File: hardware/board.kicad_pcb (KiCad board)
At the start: 2 copper layers, 80 x 55 mm, 59 parts, among them IC1 DW01A, J1 Conn_01x04_Female, J2 Conn_01x04_Female, J3 Conn_01x04_Female, J4 Conn_01x06_Female, J5 Conn_01x14, J6 Micro_SD_Card, P1 USB_C_Plug_USB2.0, Q1 AO3401A, Q2 FS8205A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

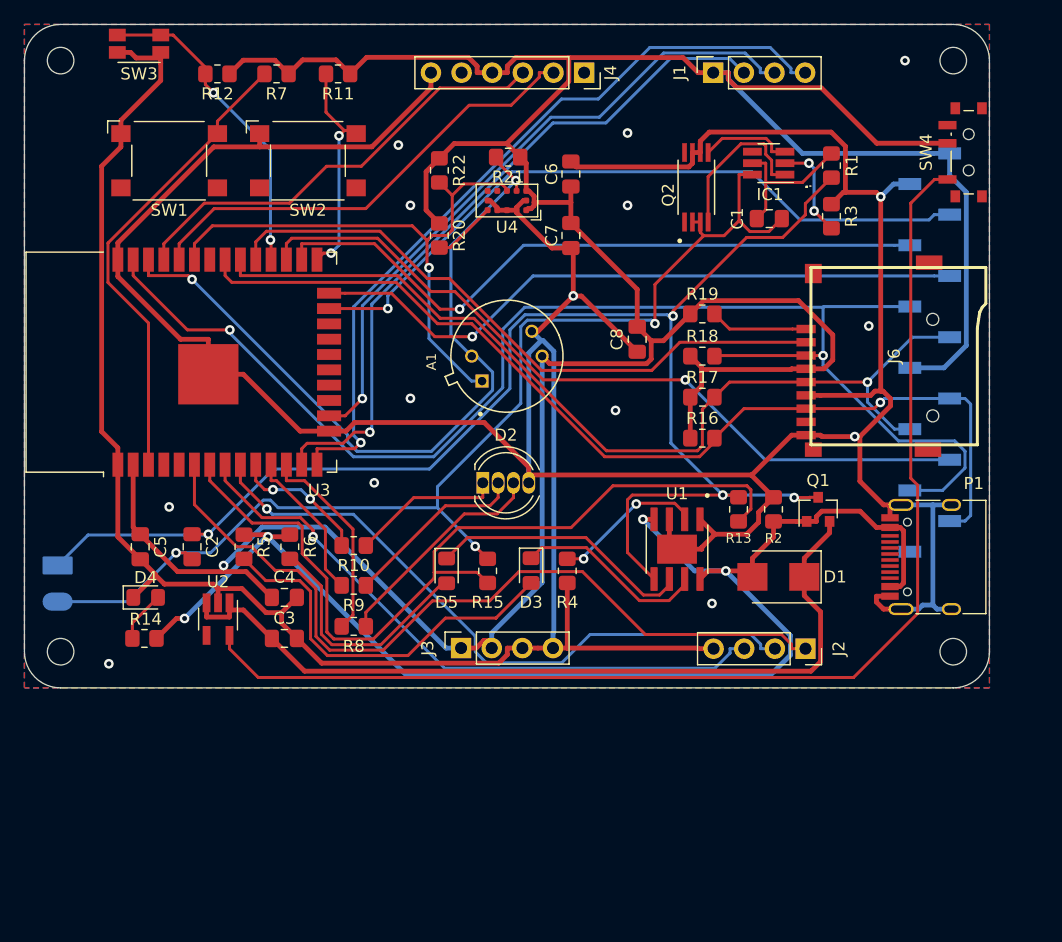
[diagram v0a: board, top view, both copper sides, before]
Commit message: Silkscreen markings added + Minor changes to tracks
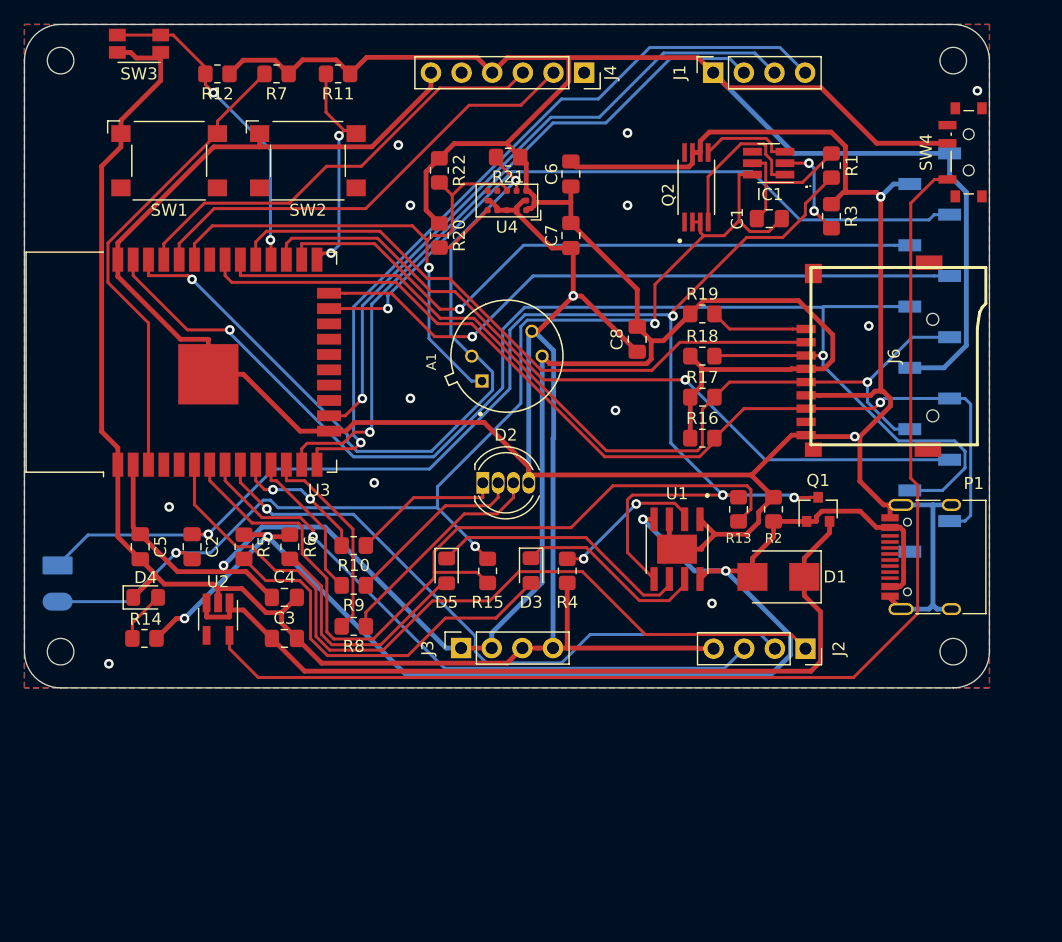
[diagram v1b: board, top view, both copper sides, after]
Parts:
- added REF**: OSHW-Logo2_7.3x6mm_SilkScreen, Symbol:OSHW-Logo2_7.3x6mm_SilkScreen, B.Cu at (111.0, 53.5)
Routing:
- net GND: track 399.5 -> 397.2 mm
- net +3V3: track 282.4 -> 281.5 mm
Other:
- board text added: "InputBlackBoxOutput"

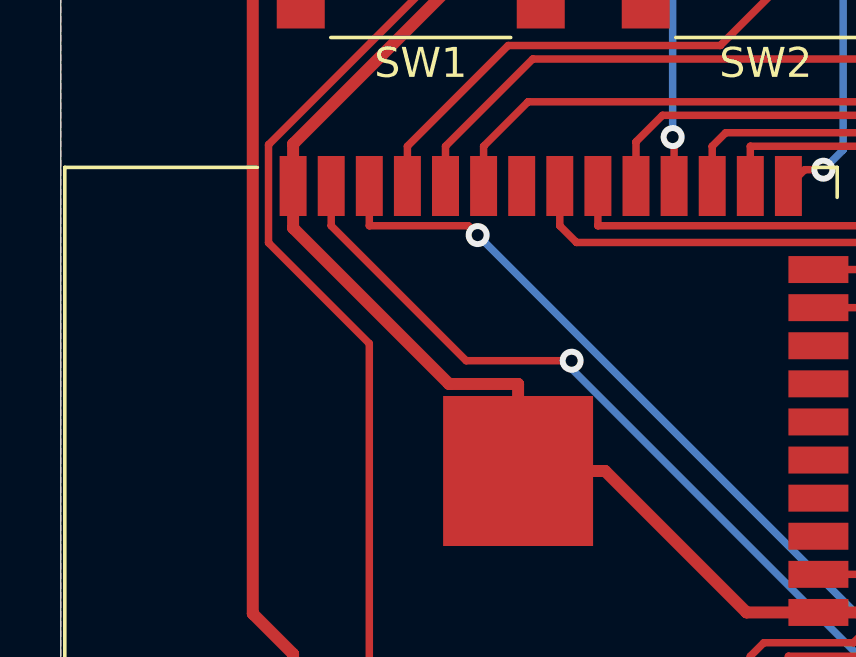
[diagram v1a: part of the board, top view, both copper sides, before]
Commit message: Minor changes to the PCB
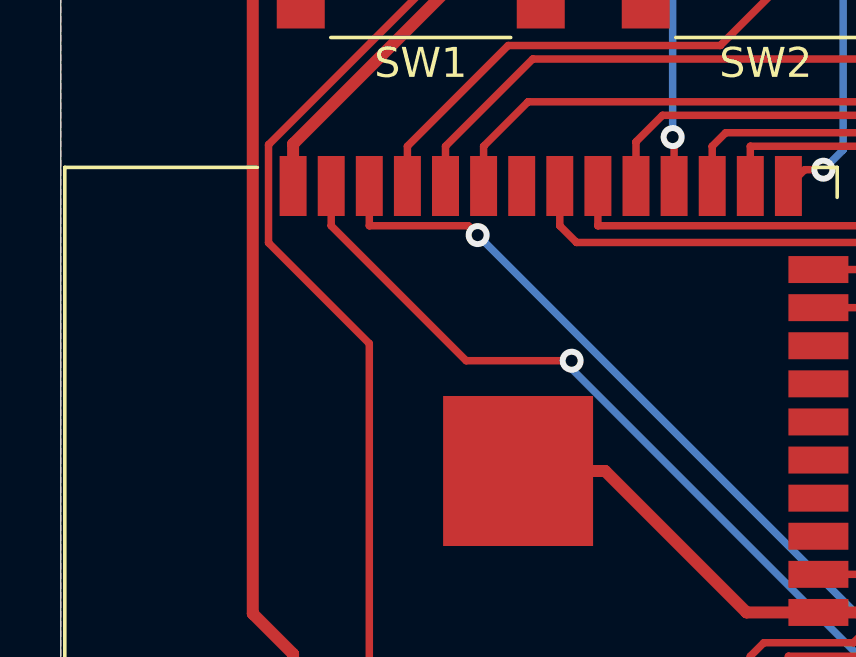
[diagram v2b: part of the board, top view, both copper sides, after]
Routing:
- net GND: track 397.2 -> 383.3 mm

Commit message: CE, FCC, WEEE and OSHW markings added to PCB
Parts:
- removed the REF** at (111.0, 53.5)
- added REF**: OSHW-Logo_5.7x6mm_SilkScreen, Symbol:OSHW-Logo_5.7x6mm_SilkScreen, B.Cu at (162.5, 64.0)
- added REF**: WEEE-Logo_4.2x6mm_SilkScreen, Symbol:WEEE-Logo_4.2x6mm_SilkScreen, B.Cu at (162.5, 70.0)
- added REF**: FCC-Logo_7.3x6mm_SilkScreen, Symbol:FCC-Logo_7.3x6mm_SilkScreen, B.Cu at (162.5, 77.0)
- added REF**: CE-Logo_8.5x6mm_SilkScreen, Symbol:CE-Logo_8.5x6mm_SilkScreen, B.Cu at (162.5, 88.0)
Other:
- board text added: "© Copyright InputBlackBoxOutput"
- board text removed: "InputBlackBoxOutput"

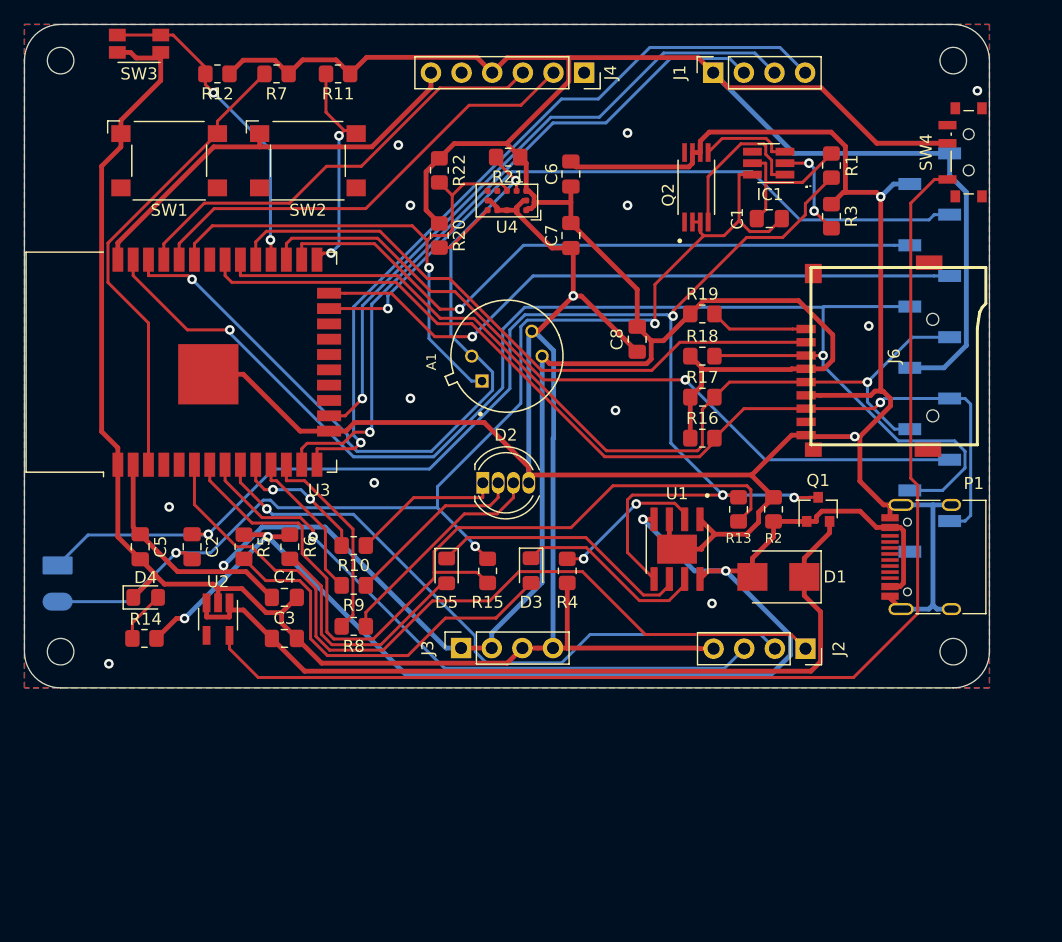
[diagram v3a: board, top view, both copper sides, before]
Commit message: Folder reorganized: hardware
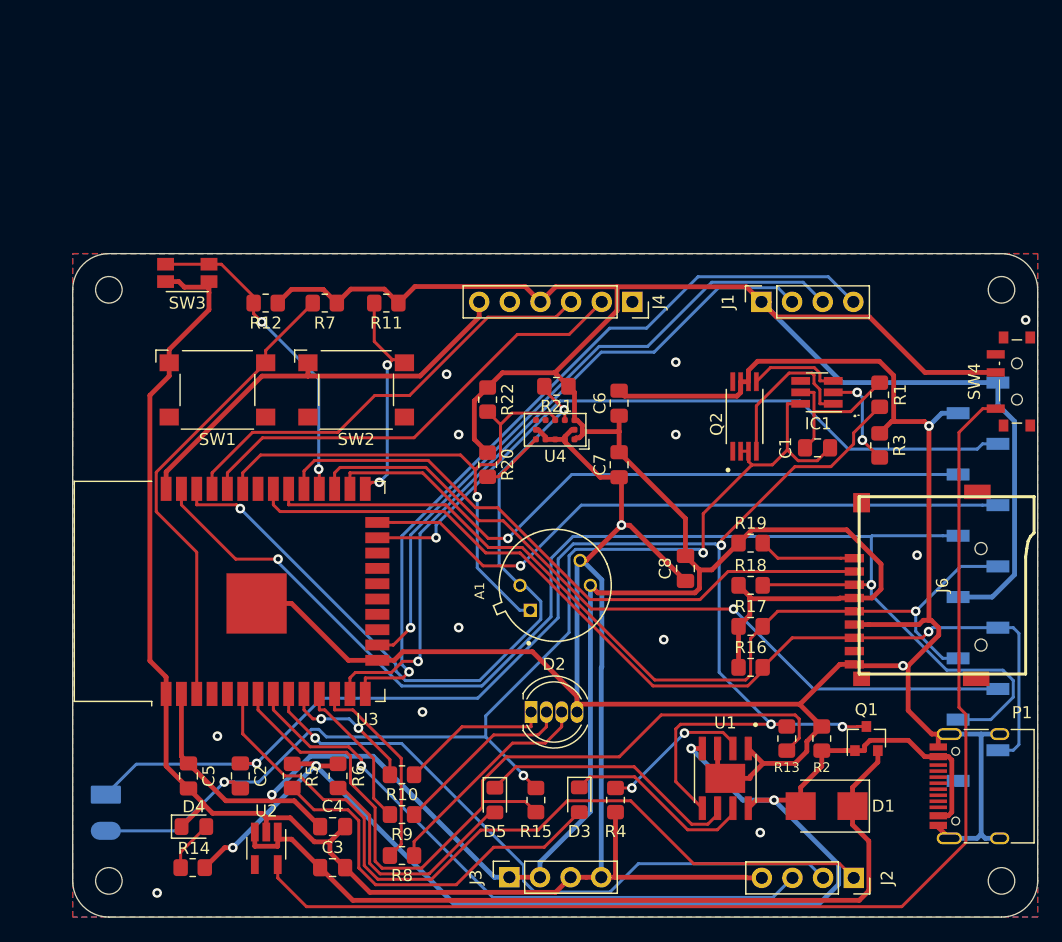
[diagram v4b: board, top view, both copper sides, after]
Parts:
- moved C6 19.4 mm to (150.3, 80.4)
- moved A1 19.4 mm to (145.0, 95.5)
- moved BT1 19.4 mm to (108.0, 111.1)
- moved C1 19.4 mm to (166.8, 84.1)
- moved C2 19.4 mm to (118.9, 111.3)
- moved C3 19.4 mm to (126.5, 118.9)
- moved C4 19.4 mm to (126.5, 115.5)
- moved C5 19.4 mm to (114.6, 111.3)
- moved C7 19.4 mm to (150.3, 85.5)
- moved C8 19.4 mm to (155.8, 94.1)
- moved D1 19.4 mm to (167.5, 113.8)
- moved D2 19.4 mm to (143.0, 106.0)
- moved D3 19.4 mm to (147.0, 113.3)
- moved D4 19.4 mm to (115.0, 115.5)
- moved D5 19.4 mm to (140.0, 113.3)
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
